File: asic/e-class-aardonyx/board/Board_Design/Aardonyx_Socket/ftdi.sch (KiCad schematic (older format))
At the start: 62 parts, among them J1 USB_B_6PIN, J17 USB_OTG, J18 Conn_1x3_M, J2 Conn_1x8, J3 Conn_1x3_M, U1 FT2232H, U16 93LC56BT-I_OT, Y1 12MHz

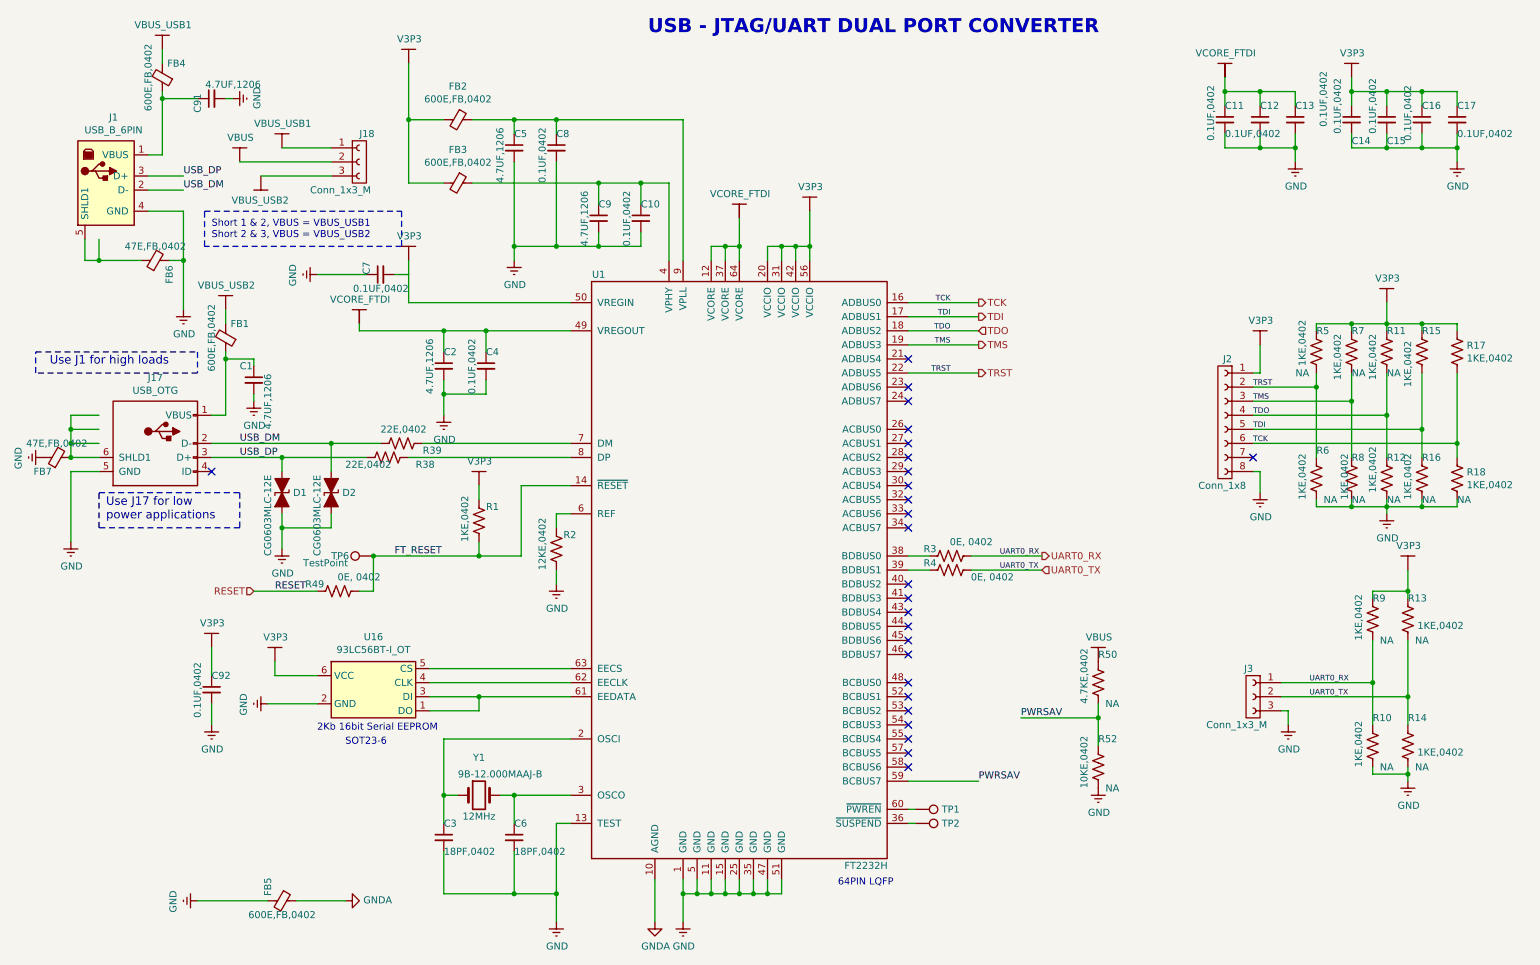
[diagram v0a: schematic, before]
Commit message: update socket compo placement
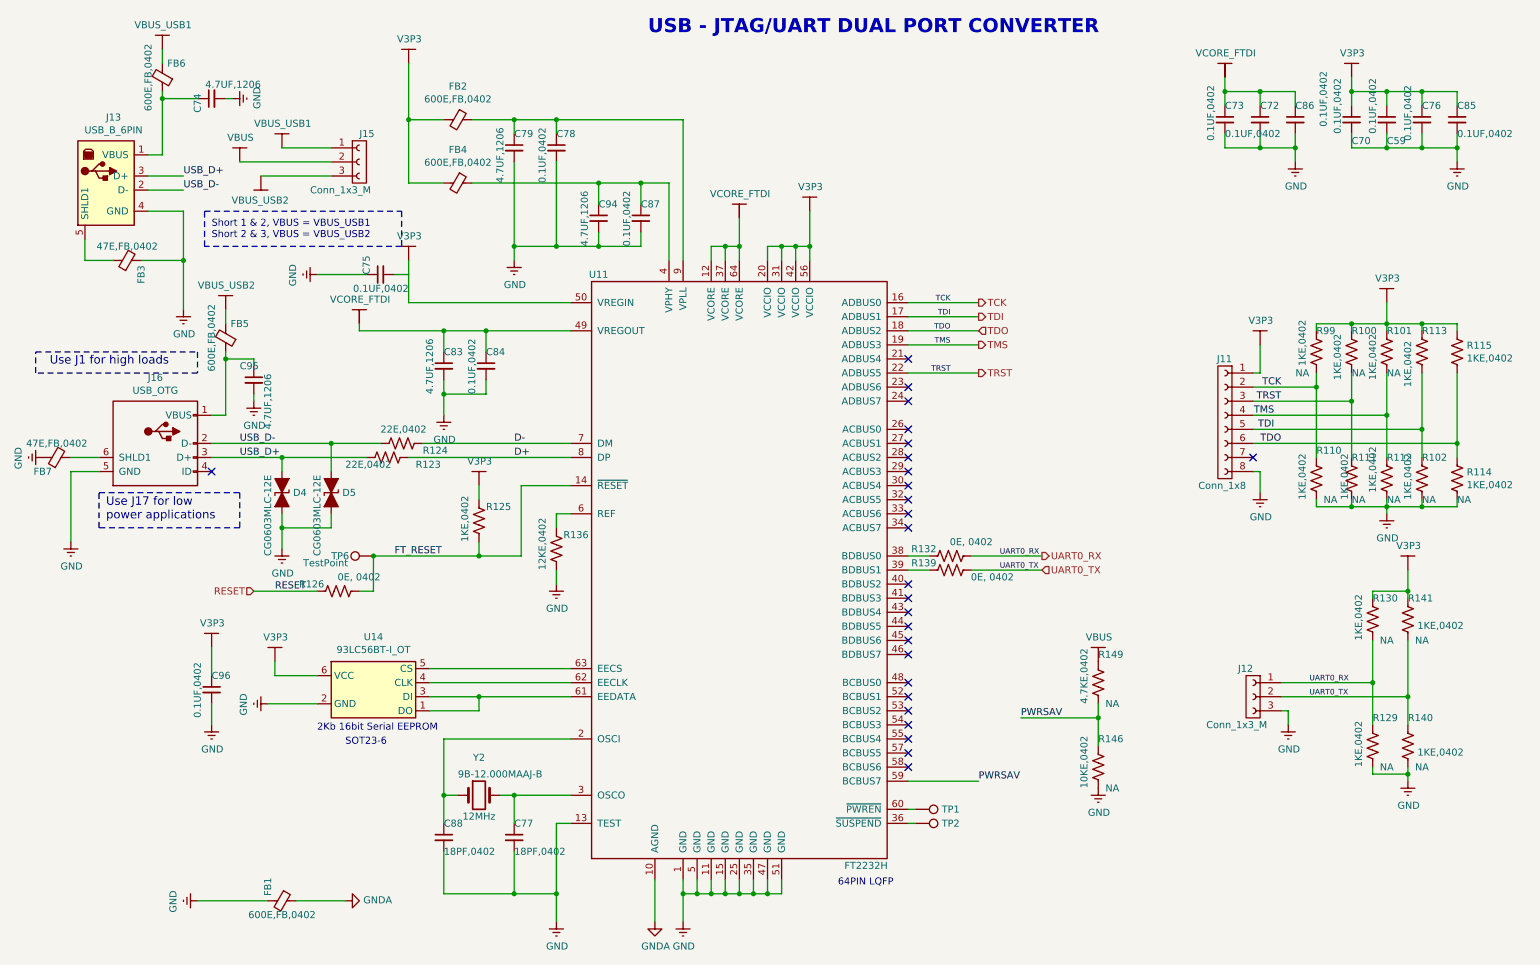
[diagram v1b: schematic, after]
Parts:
- renumbered C15 to C59, C14 to C70, C12 to C72, C11 to C73, C91 to C74, C7 to C75, C16 to C76, C6 to C77, C8 to C78, C5 to C79, C2 to C83, C4 to C84, C17 to C85, C13 to C86, C10 to C87, C3 to C88, C9 to C94, C1 to C95, C92 to C96, D1 to D4, D2 to D5, FB5 to FB1, FB6 to FB3, FB3 to FB4, FB1 to FB5, FB4 to FB6, J2 to J11, J3 to J12, J1 to J13, J18 to J15, J17 to J16, R7 to R100, R11 to R101, R16 to R102, R6 to R110, R8 to R111, R12 to R112, R15 to R113, R18 to R114, R17 to R115, R38 to R123, R39 to R124, R1 to R125, R49 to R126, R10 to R129, R9 to R130, R3 to R132, R2 to R136, R4 to R139, R14 to R140, R13 to R141, R52 to R146, R50 to R149, R5 to R99, U1 to U11, U16 to U14, Y1 to Y2
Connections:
- net TCK: now also J11.2 (Pin_2), R110.1, R99.2; no longer J11.6 (Pin_6), R114.1, R115.2
- net TDO: now also J11.6 (Pin_6), R114.1, R115.2; no longer J11.4 (Pin_4), R101.2, R112.1
- net TMS: now also J11.4 (Pin_4), R101.2, R112.1; no longer J11.3 (Pin_3), R100.2, R111.1
- net TRST: now also J11.3 (Pin_3), R100.2, R111.1; no longer J11.2 (Pin_2), R110.1, R99.2
- net D-: now reaches R124.1, U11.7 (DM)
- net D+: now reaches R123.1, U11.8 (DP)
- net USB_DM renamed USB_D-
- net USB_DP renamed USB_D+
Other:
- moved on the sheet: FB3

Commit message: updated soc back annotation
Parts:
- FB3, FB7: value 47E,FB,0402 -> 47E,FB,0603; footprint Inductor_SMD:L_0402_1005Metric -> Inductor_SMD:L_0603_1608Metric
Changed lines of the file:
@@
 P 800 3750
 F 0 "FB7" V 700 3850 50  0000 C CNN
-F 1 "47E,FB,0402" V 900 3750 50  0000 C CNN
-F 2 "Inductor_SMD:L_0402_1005Metric" V 730 3750 50  0001 C CNN
+F 1 "47E,FB,0603" V 900 3750 50  0000 C CNN
+F 2 "Inductor_SMD:L_0603_1608Metric" V 730 3750 50  0001 C CNN
 F 3 "https://www.digikey.in/product-detail/en/w%C3%BCrth-elektronik/742792608/732-1596-1-ND/1639540" H 800 3750 50  0001 C CNN
 F 4 "FERRITE BEAD 47 OHM 0603 1LN" H 800 3750 50  0001 C CNN "Description"
@@
 P 1300 2350
 F 0 "FB3" H 1200 2250 50  0000 C CNN
-F 1 "47E,FB,0402" V 1400 2350 50  0000 C CNN
-F 2 "Inductor_SMD:L_0402_1005Metric" V 1230 2350 50  0001 C CNN
+F 1 "47E,FB,0603" V 1400 2350 50  0000 C CNN
+F 2 "Inductor_SMD:L_0603_1608Metric" V 1230 2350 50  0001 C CNN
 F 3 "https://www.digikey.in/product-detail/en/w%C3%BCrth-elektronik/742792608/732-1596-1-ND/1639540" H 1300 2350 50  0001 C CNN
 F 4 "FERRITE BEAD 47 OHM 0603 1LN" H 1300 2350 50  0001 C CNN "Description"

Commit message: Back annotation
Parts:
- renumbered C95 to C55, C59 to C68, C70 to C71, C77 to C74, C74 to C83, C76 to C84, C78 to C85, C79 to C86, C75 to C87, C83 to C91, C84 to C92, C85 to C93, C86 to C94, C87 to C95, C94 to C96, C96 to C97, FB7 to FB1, FB5 to FB2, FB1 to FB3, FB6 to FB4, FB3 to FB5, FB2 to FB6, FB4 to FB7, J16 to J12, J12 to J13, J13 to J14, R123 to R113, R124 to R114, R125 to R124, R126 to R125, R129 to R140, R130 to R141, R132 to R142, R136 to R143, R139 to R144, R140 to R145, R141 to R146, R146 to R152, R149 to R153, R99 to R77, R100 to R78, R101 to R79, R102 to R80, R110 to R81, R111 to R82, R112 to R83, R113 to R84, R114 to R85, R115 to R86, U11 to U10, U14 to U15
